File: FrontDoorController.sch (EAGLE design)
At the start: 8 parts

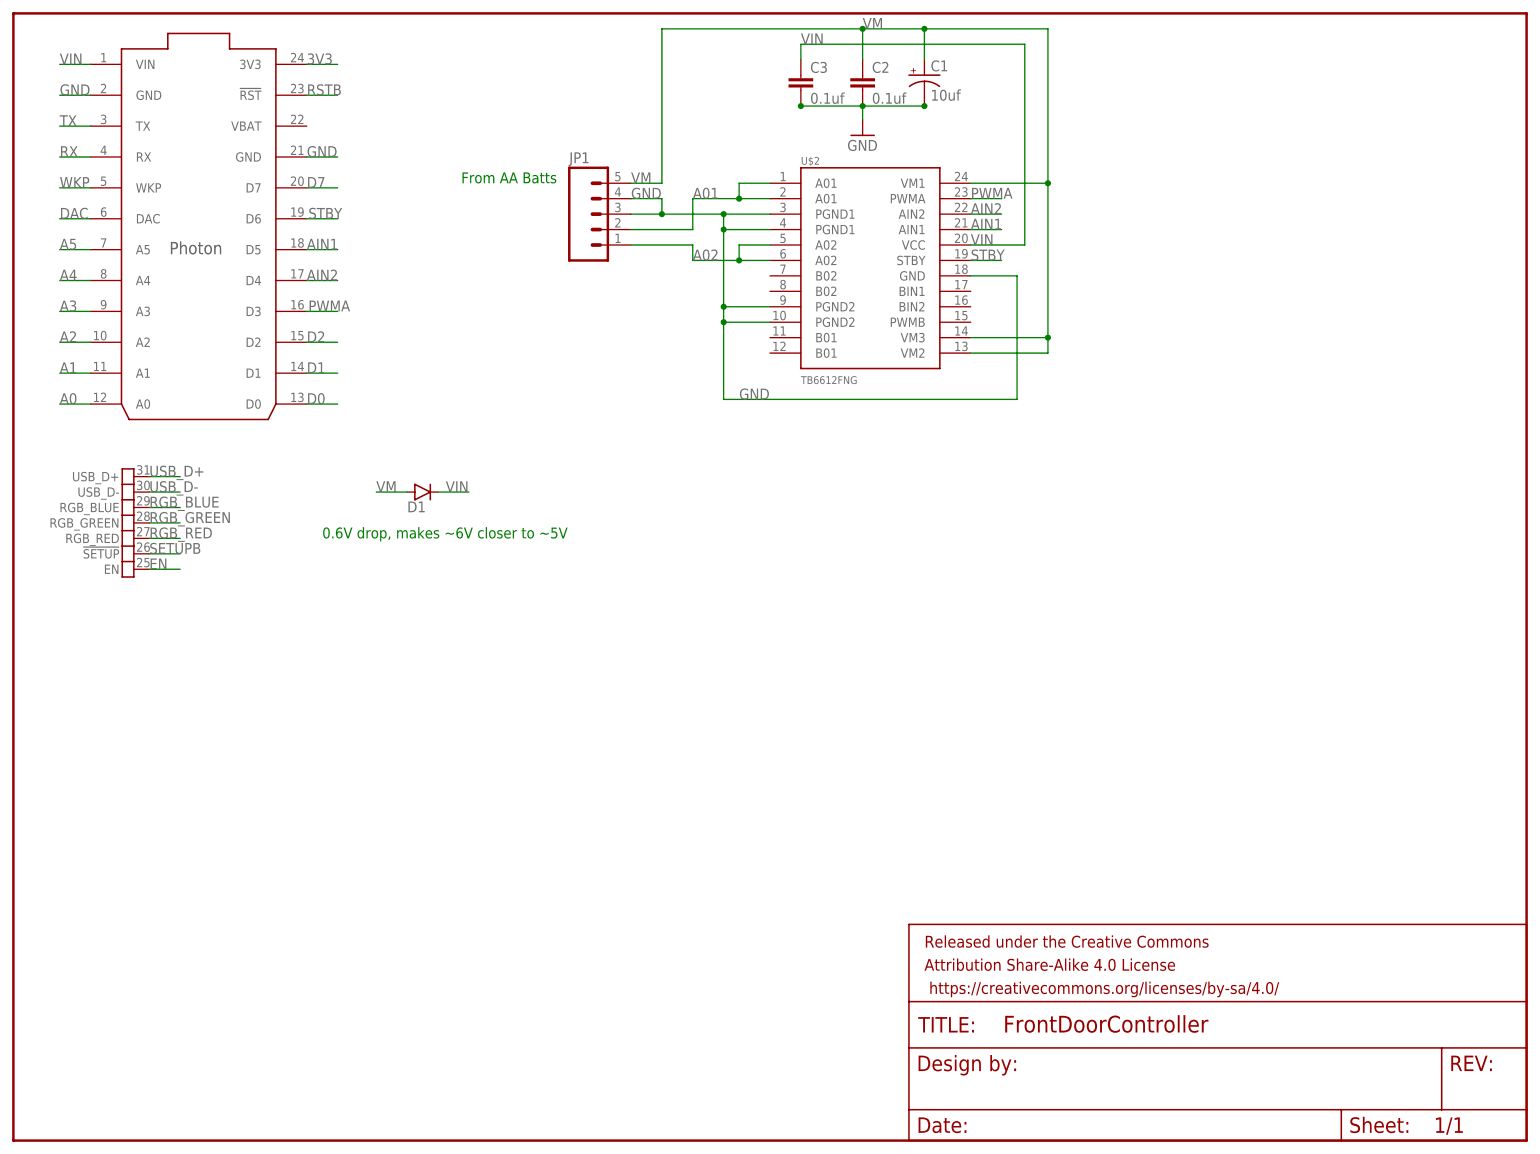
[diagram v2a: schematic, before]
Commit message: Door_Control_PCB: Add Photon through holes
Add in an additional part for the Photon through-hole connections.  This
can be used to attach the Photon to the board without soldering it down.
Also reconnect the wires to the new Photon holes and clean up the
schematic a bit.
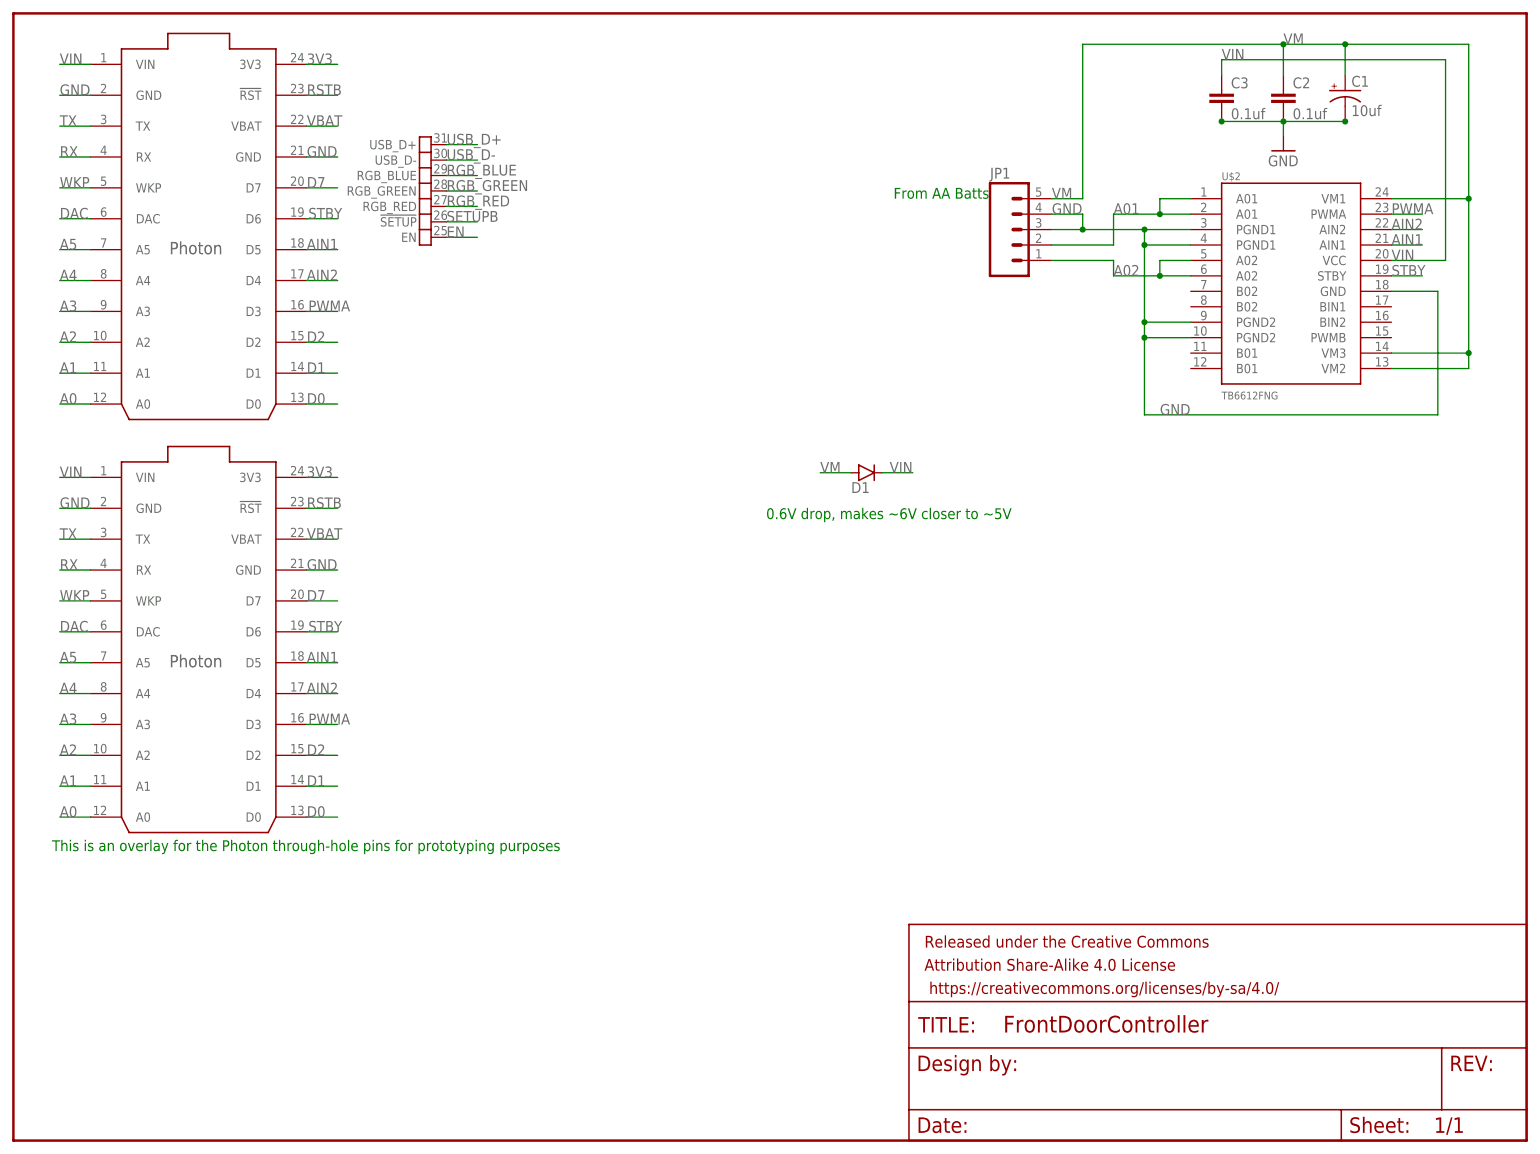
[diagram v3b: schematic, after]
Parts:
- added U$3: PHOTON_WITH_HEADERS, Spark:PHOTON_WITH_HEADERS
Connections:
- new net VBAT: U$1G$1.VBAT, U$3.VBAT
- net 3V3: now also U$3.3V3
- net A0: now also U$3.A0
- net A1: now also U$3.A1
- net A2: now also U$3.A2
- net A3: now also U$3.A3
- net A4: now also U$3.A4
- net A5: now also U$3.A5
- net AIN1: now also U$3.D5
- net AIN2: now also U$3.D4
- net D0: now also U$3.D0
- net D1: now also U$3.D1
- net D2: now also U$3.D2
- net D7: now also U$3.D7
- net DAC: now also U$3.DAC
- net GND: now also U$3.GND@2, U$3.GND@21
- net PWMA: now also U$3.D3
- net RSTB: now also U$3.!RST
- net RX: now also U$3.RX
- net STBY: now also U$3.D6
- net TX: now also U$3.TX
- net VIN: now also U$3.VIN
- net WKP: now also U$3.WKP
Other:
- note added: "This is an overlay for the Photon through-hole pins for prototyping purposes"
- moved on the sheet: C1, C2, C3, D1, JP1, U$2

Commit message: Door_Control_PCB: Add more header pins
Add more header pins to be able to measure all voltages, and connect to
the limit switches on the Lockitron to log the deadbolt position.  Also
reroute the motor drive wires to not go through the Photon through hole
pins and make the wires larger to drive more current.
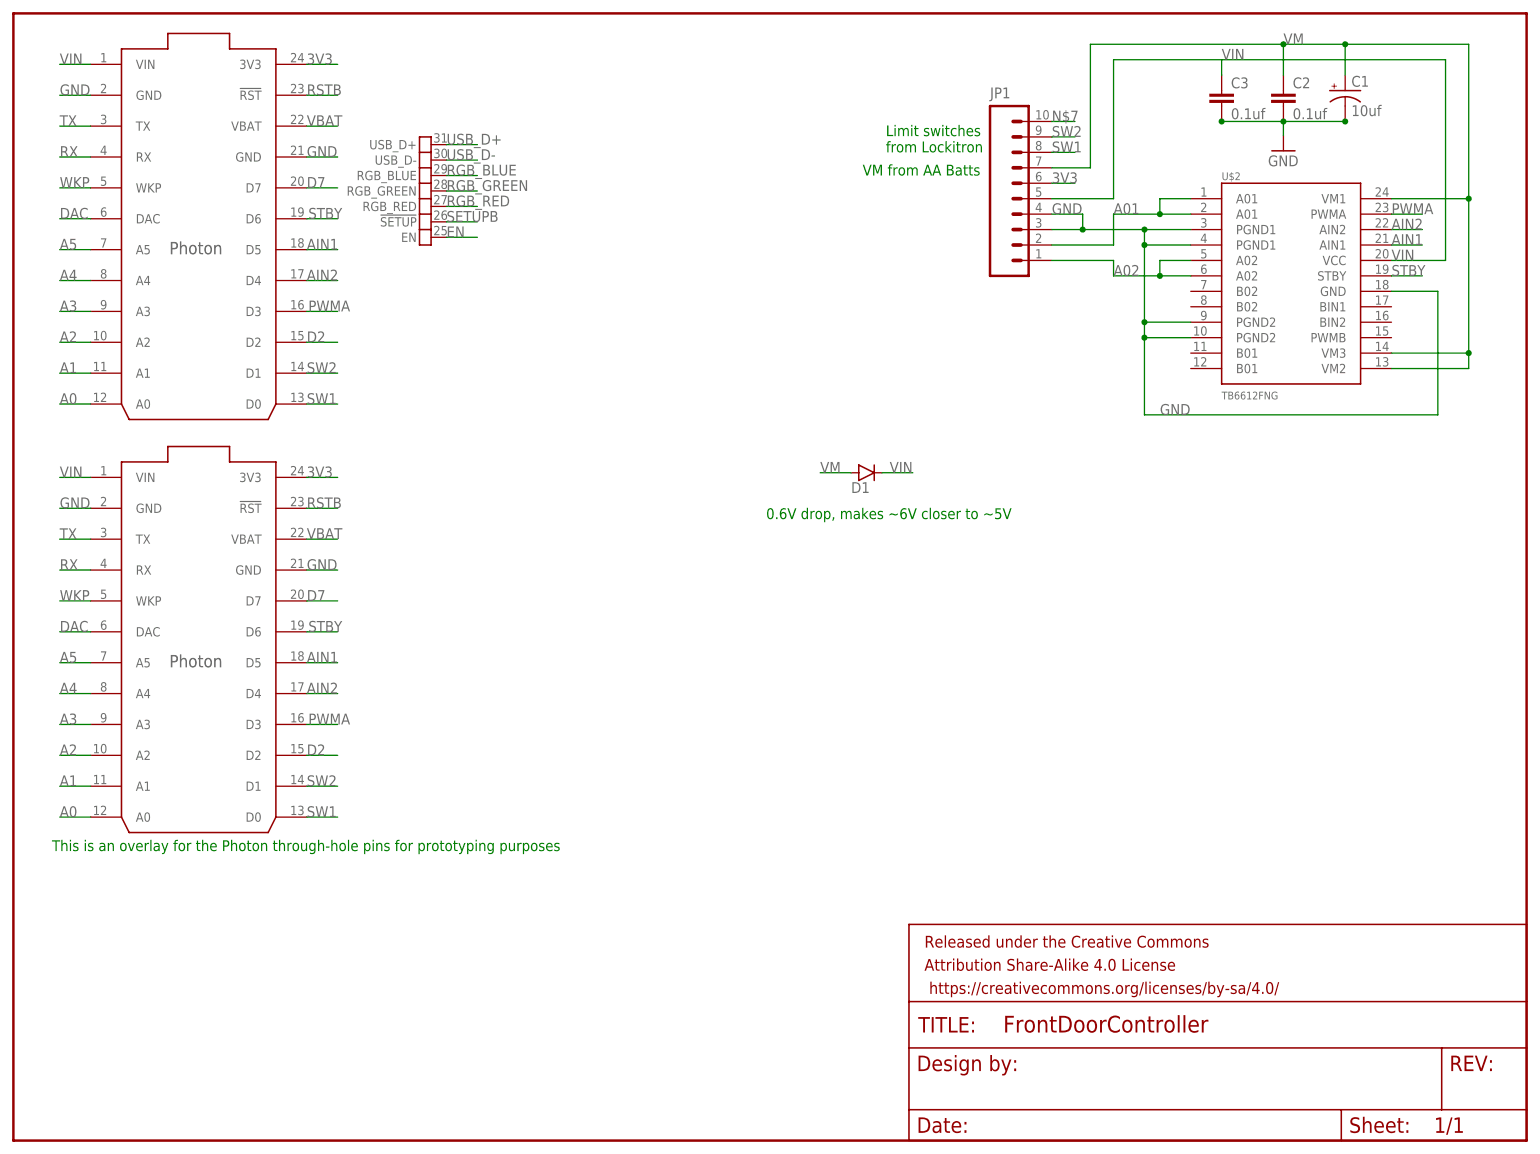
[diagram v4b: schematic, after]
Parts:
- JP1: device SparkFun-Connectors:M05PTH -> SparkFun-Connectors:M10LOCK
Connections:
- removed net D0: U$1G$1.D0, U$3.D0
- removed net D1: U$1G$1.D1, U$3.D1
- new net N$7: JP1.10
- new net SW1: JP1.8, U$1G$1.D0, U$3.D0
- new net SW2: JP1.9, U$1G$1.D1, U$3.D1
- net 3V3: now also JP1.6
- net VIN: now also JP1.5
- net VM: now also JP1.7; no longer JP1.5
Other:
- note added: "Limit switches from Lockitron"
- note added: "VM from AA Batts"
- note removed: "From AA Batts"
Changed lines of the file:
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@@
 <setting verticaltext="up"/>
 </settings>
-<grid distance="0.05" unitdist="inch" unit="inch" style="lines" multiple="1" display="no" altdistance="0.001" altunitdist="inch" altunit="inch"/>
+<grid distance="0.05" unitdist="inch" unit="inch" style="lines" multiple="1" display="no" altdistance="0.025" altunitdist="inch" altunit="inch"/>
 <layers>
 <layer number="1" name="Top" color="4" fill="1" visible="no" active="no"/>
@@
 <part name="C3" library="SparkFun-Capacitors" deviceset="CAP" device="0402-CAP" value="0.1uf"/>
 <part name="GND1" library="SparkFun-Aesthetics" deviceset="GND" device=""/>
-<part name="JP1" library="SparkFun-Connectors" deviceset="M05" device="PTH"/>
+<part name="JP1" library="SparkFun-Connectors" deviceset="M10" device="LOCK"/>
 <part name="D1" library="SparkFun-DiscreteSemi" deviceset="DIODE" device="PTH"/>
 <part name="U$3" library="Spark" deviceset="PHOTON" device="_WITH_HEADERS"/>
@@
 <sheet>
 <plain>
-<text x="144.78" y="154.94" size="1.778" layer="91">From AA Batts</text>
+<text x="139.7" y="158.75" size="1.778" layer="91">VM from AA Batts</text>
 <text x="123.825" y="102.235" size="1.778" layer="91">0.6V drop, makes ~6V closer to ~5V</text>
 <text x="6.35" y="47.625" size="1.778" layer="91">This is an overlay for the Photon through-hole pins for prototyping purposes</text>
+<text x="143.51" y="162.56" size="1.778" layer="91">Limit switches
+from Lockitron</text>
 </plain>
 <instances>
@@
 <instance part="C3" gate="G$1" x="198.755" y="170.18"/>
 <instance part="GND1" gate="1" x="208.915" y="162.814"/>
-<instance part="JP1" gate="G$1" x="163.195" y="149.86"/>
+<instance part="JP1" gate="G$1" x="160.655" y="162.56"/>
 <instance part="D1" gate="G$1" x="140.335" y="109.855" smashed="yes">
 <attribute name="NAME" x="137.795" y="106.5276" size="1.778" layer="95"/>
@@
 <label x="226.695" y="144.78" size="1.778" layer="95"/>
 <label x="198.755" y="177.8" size="1.778" layer="95"/>
+<wire x1="198.755" y1="177.8" x2="180.975" y2="177.8" width="0.1524" layer="91"/>
+<wire x1="180.975" y1="177.8" x2="180.975" y2="154.94" width="0.1524" layer="91"/>
+<pinref part="JP1" gate="G$1" pin="5"/>
+<wire x1="180.975" y1="154.94" x2="170.815" y2="154.94" width="0.1524" layer="91"/>
 </segment>
 <segment>
@@
 <label x="48.26" y="109.093" size="1.778" layer="95"/>
 </segment>
+<segment>
+<pinref part="JP1" gate="G$1" pin="6"/>
+<wire x1="170.815" y1="157.48" x2="174.625" y2="157.48" width="0.1524" layer="91"/>
+<label x="170.815" y="157.48" size="1.778" layer="95"/>
+</segment>
 </net>
 <net name="RSTB" class="0">
@@
 <wire x1="48.26" y1="63.373" x2="53.34" y2="63.373" width="0.1524" layer="91"/>
 <label x="48.26" y="63.373" size="1.778" layer="95"/>
-</segment>
-</net>
-<net name="D1" class="0">
-<segment>
-<pinref part="U$1" gate="G$1" pin="D1"/>
-<wire x1="48.26" y1="126.238" x2="53.34" y2="126.238" width="0.1524" layer="91"/>
-<label x="48.26" y="126.238" size="1.778" layer="95"/>
-</segment>
-<segment>
-<pinref part="U$3" gate="G$1" pin="D1"/>
-<wire x1="48.26" y1="58.293" x2="53.34" y2="58.293" width="0.1524" layer="91"/>
-<label x="48.26" y="58.293" size="1.778" layer="95"/>
-</segment>
-</net>
-<net name="D0" class="0">
-<segment>
-<pinref part="U$1" gate="G$1" pin="D0"/>
-<wire x1="48.26" y1="121.158" x2="53.34" y2="121.158" width="0.1524" layer="91"/>
-<label x="48.26" y="121.158" size="1.778" layer="95"/>
-</segment>
-<segment>
-<pinref part="U$3" gate="G$1" pin="D0"/>
-<wire x1="48.26" y1="53.213" x2="53.34" y2="53.213" width="0.1524" layer="91"/>
-<label x="48.26" y="53.213" size="1.778" layer="95"/>
 </segment>
 </net>
@@
 <pinref part="C2" gate="G$1" pin="1"/>
 <wire x1="208.915" y1="180.34" x2="208.915" y2="175.26" width="0.1524" layer="91"/>
-<pinref part="JP1" gate="G$1" pin="5"/>
-<wire x1="170.815" y1="154.94" x2="175.895" y2="154.94" width="0.1524" layer="91"/>
-<label x="170.815" y="154.94" size="1.778" layer="95"/>
-<wire x1="208.915" y1="180.34" x2="175.895" y2="180.34" width="0.1524" layer="91"/>
-<wire x1="175.895" y1="180.34" x2="175.895" y2="154.94" width="0.1524" layer="91"/>
+<wire x1="208.915" y1="180.34" x2="177.165" y2="180.34" width="0.1524" layer="91"/>
 <junction x="219.075" y="180.34"/>
 <junction x="208.915" y="180.34"/>
+<pinref part="JP1" gate="G$1" pin="7"/>
+<wire x1="170.815" y1="160.02" x2="177.165" y2="160.02" width="0.1524" layer="91"/>
+<wire x1="177.165" y1="160.02" x2="177.165" y2="180.34" width="0.1524" layer="91"/>
 </segment>
 <segment>
@@
 </segment>
 </net>
+<net name="SW1" class="0">
+<segment>
+<pinref part="JP1" gate="G$1" pin="8"/>
+<wire x1="170.815" y1="162.56" x2="174.625" y2="162.56" width="0.1524" layer="91"/>
+<label x="170.815" y="162.56" size="1.778" layer="95"/>
+</segment>
+<segment>
+<pinref part="U$1" gate="G$1" pin="D0"/>
+<wire x1="48.26" y1="121.158" x2="53.34" y2="121.158" width="0.1524" layer="91"/>
+<label x="48.26" y="121.158" size="1.778" layer="95"/>
+</segment>
+<segment>
+<pinref part="U$3" gate="G$1" pin="D0"/>
+<wire x1="48.26" y1="53.213" x2="53.34" y2="53.213" width="0.1524" layer="91"/>
+<label x="48.26" y="53.213" size="1.778" layer="95"/>
+</segment>
+</net>
+<net name="SW2" class="0">
+<segment>
+<pinref part="JP1" gate="G$1" pin="9"/>
+<wire x1="170.815" y1="165.1" x2="174.625" y2="165.1" width="0.1524" layer="91"/>
+<label x="170.815" y="165.1" size="1.778" layer="95"/>
+</segment>
+<segment>
+<pinref part="U$1" gate="G$1" pin="D1"/>
+<wire x1="48.26" y1="126.238" x2="53.34" y2="126.238" width="0.1524" layer="91"/>
+<label x="48.26" y="126.238" size="1.778" layer="95"/>
+</segment>
+<segment>
+<pinref part="U$3" gate="G$1" pin="D1"/>
+<wire x1="48.26" y1="58.293" x2="53.34" y2="58.293" width="0.1524" layer="91"/>
+<label x="48.26" y="58.293" size="1.778" layer="95"/>
+</segment>
+</net>
+<net name="N$7" class="0">
+<segment>
+<pinref part="JP1" gate="G$1" pin="10"/>
+<wire x1="170.815" y1="167.64" x2="174.625" y2="167.64" width="0.1524" layer="91"/>
+<label x="170.815" y="167.64" size="1.778" layer="95"/>
+</segment>
+</net>
